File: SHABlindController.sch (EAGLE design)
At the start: 39 parts, among them IC1 SPARKCORE, IC2 HLKPM01, IC3 RXB1, Q1 2N7002, Q2 2N7002

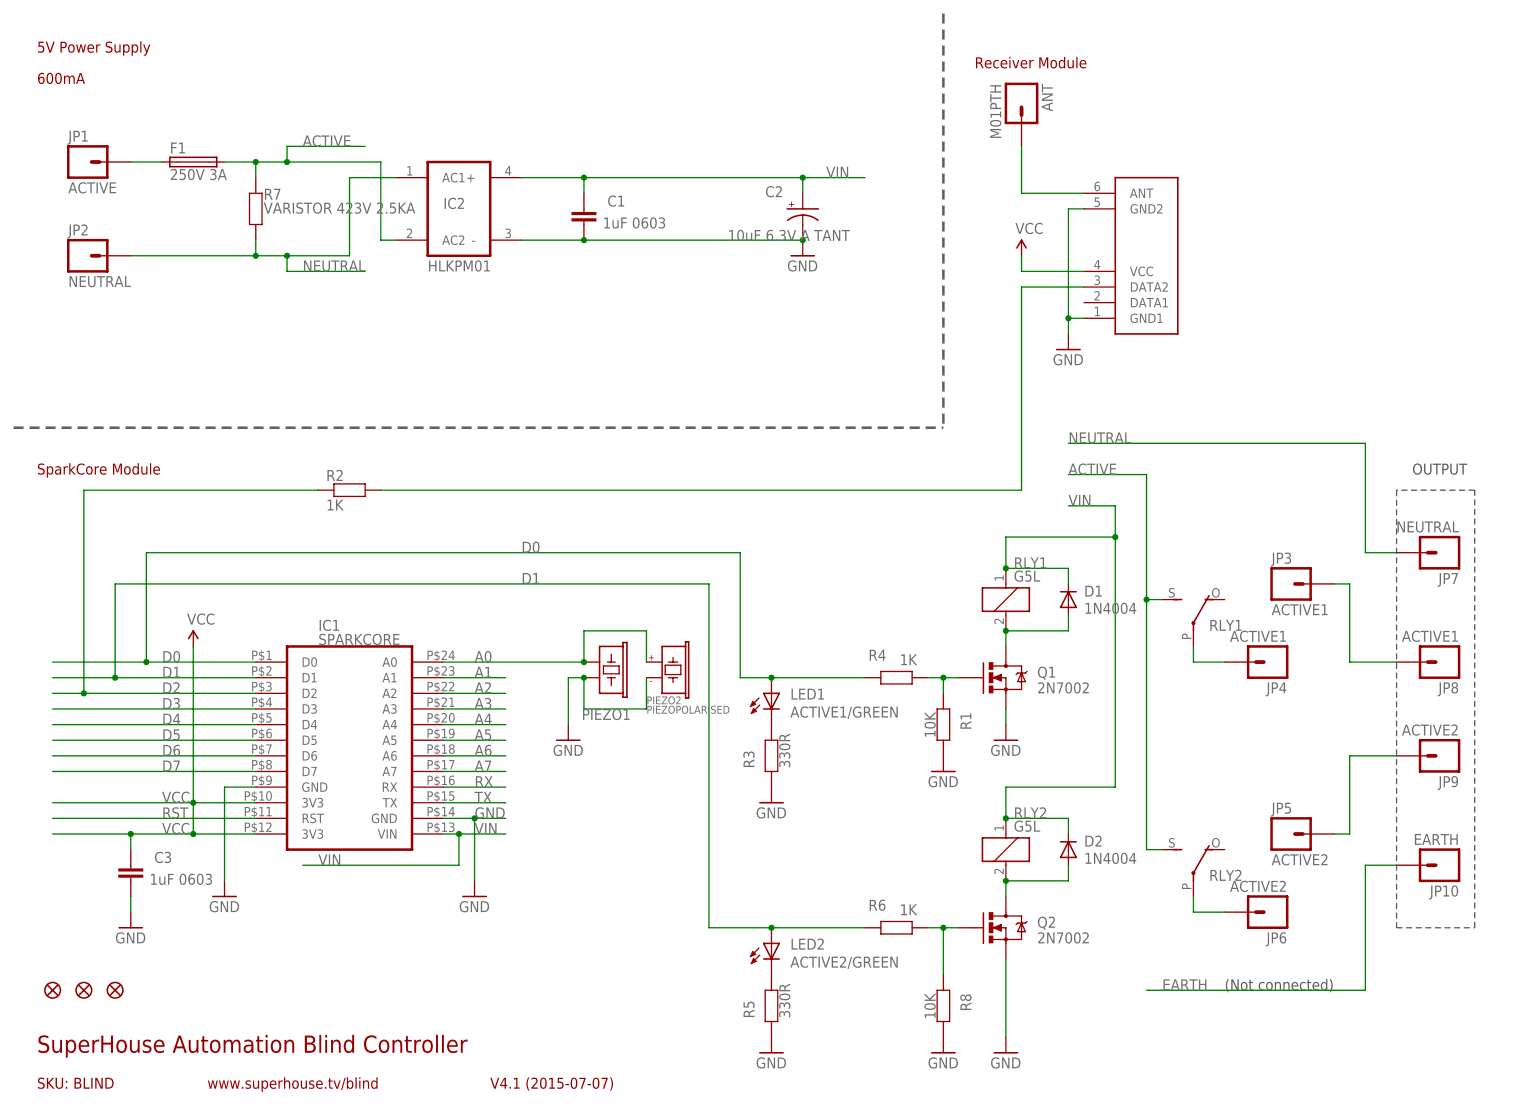
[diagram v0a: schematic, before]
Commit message: Added solder-jumper to link GND and Neutral Reduced spacing between relays Increased length of fuse footprint
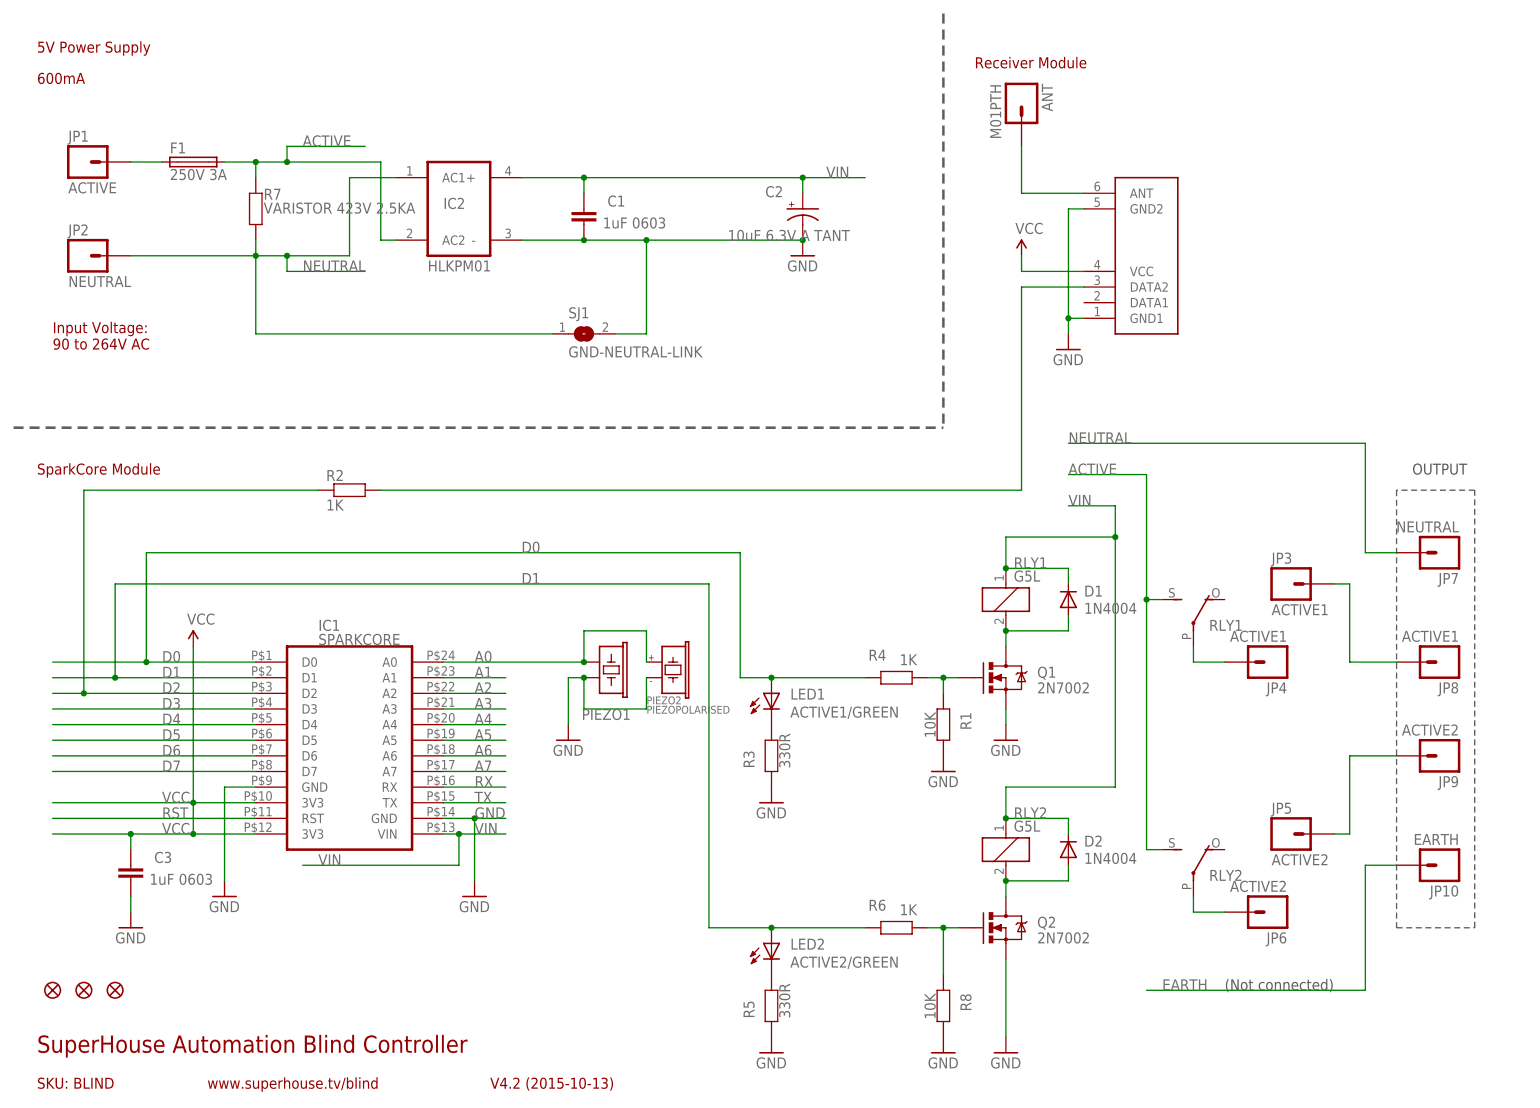
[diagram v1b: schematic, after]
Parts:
- added SJ1: GND-NEUTRAL-LINK, freetronics-master-v1.1:SJ
- F1: device freetronics-jon:PICOFUSE -> freetronics-jon:PICOFUSEH
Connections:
- net GND: now also SJ1.2
- net NEUTRAL: now also SJ1.1
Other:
- note added: "Input Voltage: 90 to 264V AC"
- note added: "V4.2 (2015-10-13)"
- note removed: "V4.1 (2015-07-07)"
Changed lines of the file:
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@@
 <part name="PIEZO2" library="freetronics-jon" deviceset="PIEZOPOLARISED" device=""/>
 <part name="IC2" library="freetronics-jon" deviceset="HLKPM01" device=""/>
-<part name="F1" library="freetronics-jon" deviceset="PICOFUSE" device="" value="250V 3A"/>
+<part name="F1" library="freetronics-jon" deviceset="PICOFUSE" device="H" value="250V 3A"/>
+<part name="SJ1" library="freetronics-master-v1.1" deviceset="SJ" device="" value="GND-NEUTRAL-LINK"/>
 </parts>
 <sheets>
@@
 <text x="7.62" y="170.18" size="1.778" layer="94">600mA</text>
 <text x="7.62" y="12.7" size="2.794" layer="94">SuperHouse Automation Blind Controller</text>
-<text x="81.28" y="6.858" size="1.778" layer="94">V4.1 (2015-07-07)</text>
+<text x="81.28" y="6.858" size="1.778" layer="94">V4.2 (2015-10-13)</text>
 <text x="35.306" y="6.858" size="1.778" layer="94">www.superhouse.tv/blind</text>
 <frame x1="0" y1="0" x2="248.92" y2="185.42" columns="8" rows="5" layer="94"/>
@@
 <text x="231.14" y="106.68" size="1.778" layer="97">OUTPUT</text>
 <text x="200.66" y="22.86" size="1.778" layer="97">(Not connected)</text>
+<text x="10.16" y="127" size="1.778" layer="94">Input Voltage:
+90 to 264V AC</text>
 </plain>
 <instances>
@@
 <instance part="IC2" gate="G$1" x="76.2" y="149.86"/>
 <instance part="F1" gate="1" x="33.02" y="157.48"/>
+<instance part="SJ1" gate="1" x="96.52" y="129.54"/>
 </instances>
 <busses>
@@
 <net name="GND" class="0">
 <segment>
-<wire x1="96.52" y1="144.78" x2="132.08" y2="144.78" width="0.1524" layer="91"/>
+<wire x1="96.52" y1="144.78" x2="106.68" y2="144.78" width="0.1524" layer="91"/>
 <junction x="96.52" y="144.78"/>
 <pinref part="C2" gate="G$1" pin="-"/>
 <pinref part="C1" gate="G$1" pin="2"/>
+<wire x1="106.68" y1="144.78" x2="132.08" y2="144.78" width="0.1524" layer="91"/>
 <wire x1="86.36" y1="144.78" x2="96.52" y2="144.78" width="0.1524" layer="91"/>
 <pinref part="GND10" gate="1" pin="GND"/>
 <junction x="132.08" y="144.78"/>
 <pinref part="IC2" gate="G$1" pin="-"/>
+<pinref part="SJ1" gate="1" pin="2"/>
+<wire x1="101.6" y1="129.54" x2="106.68" y2="129.54" width="0.1524" layer="91"/>
+<wire x1="106.68" y1="129.54" x2="106.68" y2="144.78" width="0.1524" layer="91"/>
+<junction x="106.68" y="144.78"/>
 </segment>
 <segment>
@@
 <wire x1="48.26" y1="139.7" x2="60.96" y2="139.7" width="0.1524" layer="91"/>
 <junction x="48.26" y="142.24"/>
+<pinref part="SJ1" gate="1" pin="1"/>
+<wire x1="91.44" y1="129.54" x2="43.18" y2="129.54" width="0.1524" layer="91"/>
+<wire x1="43.18" y1="129.54" x2="43.18" y2="142.24" width="0.1524" layer="91"/>
 </segment>
 <segment>
@@
 </schematic>
 </drawing>
+<compatibility>
+<note version="6.3" minversion="6.2.2" severity="warning">
+Since Version 6.2.2 text objects can contain more than one line,
+which will not be processed correctly with this version.
+</note>
+</compatibility>
 </eagle>

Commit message: Layout updates
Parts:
- removed JP10: EARTH, freetronics-master-v1.1:M01PTH_LARGE
- removed JP3, JP8: ACTIVE1, freetronics-master-v1.1:M01PTH_LARGE
- removed JP5, JP9: ACTIVE2, freetronics-master-v1.1:M01PTH_LARGE
- added C4: 100nF 0603, freetronics-master-v1.1:CAP0603
- added IC4: AH180-PL-A, freetronics-jon:US1881TO92
- added LED3: ROTATE/GREEN, freetronics:LED0603
- added R10: 1K 0603, freetronics-master-v1:RESISTOR0603
- added R11, R9: 10K 0603, freetronics-master-v1:RESISTOR0603
- added R12: 10K, freetronics:RESISTOR0603
- added S2: 2P-JST-PTH, freetronics-jon:2P-JST-TH-RAPTH
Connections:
- removed net D3: IC1.D3
- removed net D4: IC1.D4
- removed net D5: IC1.D5
- removed net EARTH: JP10.1
- removed net N$7: JP3.1, JP8.1
- removed net N$8: JP5.1, JP9.1
- new net D3_BUTTON: IC1.D3, R11.1, S2.POS
- new net D4_ROTATE: IC1.D4, IC4.OUT, R10.2, R9.1
- new net D5_TYPE: IC1.D5, R12.1
- new net N$11: LED3.C, R10.1
- net GND: now also C4.2, IC4.GND, R12.2, S2.NEG
- net VCC: now also C4.1, IC4.VDD, LED3.A, R11.2, R9.2
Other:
- note added: "2.0mm JST"
- note added: "Spark Core / Particle Photon Module"
- note added: "V5.0 (2015-11-15)"
- note removed: "(Not connected)"
- note removed: "SparkCore Module"
- note removed: "V4.2 (2015-10-13)"
- moved on the sheet: ANT, C1, C2, C3, D1, D2, F1, IC2, JP4, JP6, JP7, LED1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
